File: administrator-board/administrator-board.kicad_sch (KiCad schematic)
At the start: 10 parts, among them J2 Conn_01x06, J3 Conn_01x06, SW2 SW_Push, SW3 SW_Push, SW4 SW_Push, SW5 SW_Push

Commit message: フットプリントの割り当て
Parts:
- J2, J3: footprint (none) -> Connector_JST:JST_XH_S6B-XH-A_1x06_P2.50mm_Horizontal
- R2, R3, R4, R5: footprint (none) -> Resistor_SMD:R_0603_1608Metric_Pad0.98x0.95mm_HandSolder
- SW2, SW3, SW4, SW5: footprint (none) -> Button_Switch_THT:SW_PUSH_6mm
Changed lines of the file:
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@@
 			)
 		)
-		(property "Footprint" ""
+		(property "Footprint" "Connector_JST:JST_XH_S6B-XH-A_1x06_P2.50mm_Horizontal"
 			(at 177.8 146.05 0)
 			(hide yes)
@@
 			)
 		)
-		(property "Footprint" ""
+		(property "Footprint" "Resistor_SMD:R_0603_1608Metric_Pad0.98x0.95mm_HandSolder"
 			(at 211.582 110.49 90)
 			(hide yes)
@@
 			)
 		)
-		(property "Footprint" ""
+		(property "Footprint" "Resistor_SMD:R_0603_1608Metric_Pad0.98x0.95mm_HandSolder"
 			(at 160.782 110.49 90)
 			(hide yes)
@@
 			)
 		)
-		(property "Footprint" ""
+		(property "Footprint" "Resistor_SMD:R_0603_1608Metric_Pad0.98x0.95mm_HandSolder"
 			(at 188.722 110.49 90)
 			(hide yes)
@@
 			)
 		)
-		(property "Footprint" ""
+		(property "Footprint" "Button_Switch_THT:SW_PUSH_6mm"
 			(at 195.58 99.06 0)
 			(hide yes)
@@
 			)
 		)
-		(property "Footprint" ""
+		(property "Footprint" "Connector_JST:JST_XH_S6B-XH-A_1x06_P2.50mm_Horizontal"
 			(at 219.71 144.78 0)
 			(hide yes)
@@
 			)
 		)
-		(property "Footprint" ""
+		(property "Footprint" "Button_Switch_THT:SW_PUSH_6mm"
 			(at 241.3 99.06 0)
 			(hide yes)
@@
 			)
 		)
-		(property "Footprint" ""
+		(property "Footprint" "Resistor_SMD:R_0603_1608Metric_Pad0.98x0.95mm_HandSolder"
 			(at 234.442 110.49 90)
 			(hide yes)
@@
 			)
 		)
-		(property "Footprint" ""
+		(property "Footprint" "Button_Switch_THT:SW_PUSH_6mm"
 			(at 167.64 99.06 0)
 			(hide yes)
@@
 			)
 		)
-		(property "Footprint" ""
+		(property "Footprint" "Button_Switch_THT:SW_PUSH_6mm"
 			(at 218.44 99.06 0)
 			(hide yes)

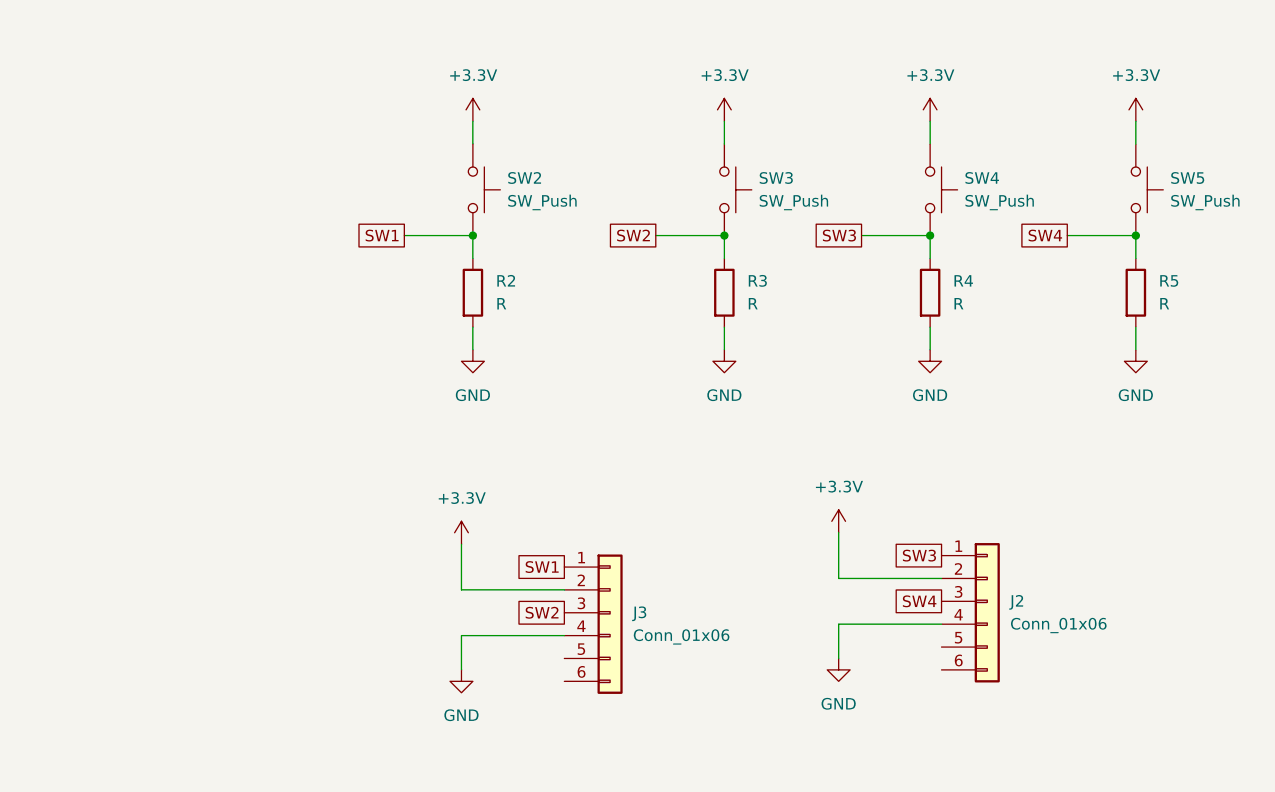
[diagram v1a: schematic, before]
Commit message: LED追加
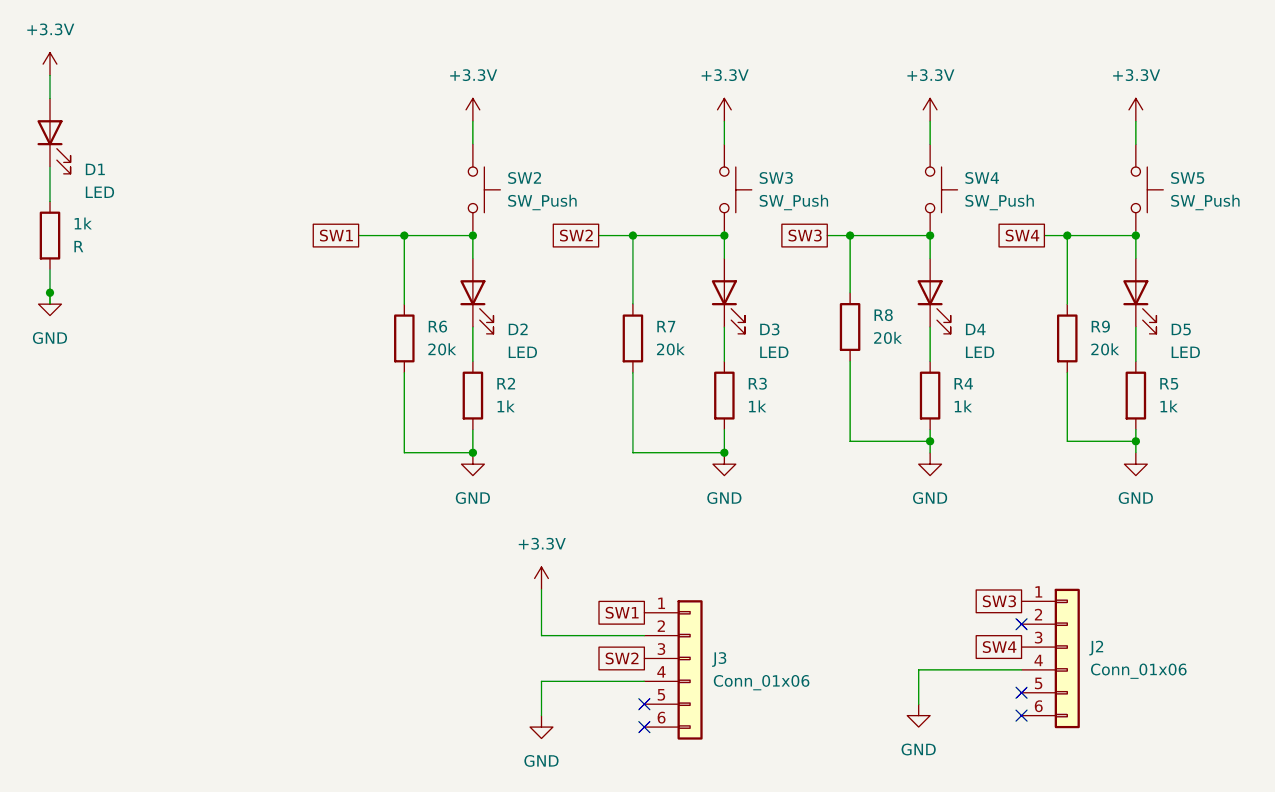
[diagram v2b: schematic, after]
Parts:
- added 1k: R, Resistor_SMD:R_0603_1608Metric_Pad0.98x0.95mm_HandSolder, symbol Device:R
- added D1, D2, D3, D4, D5: LED, symbol Device:LED
- added R6, R7, R8, R9: 20k, Resistor_SMD:R_0603_1608Metric_Pad0.98x0.95mm_HandSolder, symbol Device:R
- R2, R3, R4, R5: value R -> 1k
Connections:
- net +3.3V: now also D1.2 (A); no longer J2.2 (Pin_2)
- net GND: now also 1k.2, R6.2, R7.2, R8.2, R9.2
- net SW1: now also D2.2 (A), R6.1; no longer R2.1
- net SW2: now also D3.2 (A), R7.1; no longer R3.1
- net SW3: now also D4.2 (A), R8.1; no longer R4.1
- net SW4: now also D5.2 (A), R9.1; no longer R5.1
- new net: D4.1 (K), R4.1
- new net: D3.1 (K), R3.1
- new net: 1k.1, D1.1 (K)
- new net: D2.1 (K), R2.1
- new net: D5.1 (K), R5.1
- no-connect marks 0 -> 5
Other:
- moved on the sheet: J2, J3, R2, R3, R4, R5

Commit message: GNDの色塗りまで終わった
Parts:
- D1, D2, D3, D4, D5: footprint (none) -> LED_SMD:LED_0603_1608Metric_Pad1.05x0.95mm_HandSolder
- R1: renamed from 1k; value R -> 1k
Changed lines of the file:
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@@
 			)
 		)
-		(property "Footprint" ""
+		(property "Footprint" "LED_SMD:LED_0603_1608Metric_Pad1.05x0.95mm_HandSolder"
 			(at 190.5 110.49 0)
 			(hide yes)
@@
 		(dnp no)
 		(fields_autoplaced yes)
-		(property "Reference" "1k"
+		(property "Reference" "R1"
 			(at 118.11 102.8699 0)
 			(show_name no)
@@
 			)
 		)
-		(property "Value" "R"
+		(property "Value" "1k"
 			(at 118.11 105.4099 0)
 			(show_name no)
@@
 			(project "administrator-board"
 				(path "/d3296edd-98d5-4d49-a411-50c326b4086d"
-					(reference "1k")
+					(reference "R1")
 					(unit 1)
 				)
@@
 			)
 		)
-		(property "Footprint" ""
+		(property "Footprint" "LED_SMD:LED_0603_1608Metric_Pad1.05x0.95mm_HandSolder"
 			(at 115.57 92.71 0)
 			(hide yes)
@@
 			)
 		)
-		(property "Footprint" ""
+		(property "Footprint" "LED_SMD:LED_0603_1608Metric_Pad1.05x0.95mm_HandSolder"
 			(at 162.56 110.49 0)
 			(hide yes)
@@
 			)
 		)
-		(property "Footprint" ""
+		(property "Footprint" "LED_SMD:LED_0603_1608Metric_Pad1.05x0.95mm_HandSolder"
 			(at 236.22 110.49 0)
 			(hide yes)
@@
 			)
 		)
-		(property "Footprint" ""
+		(property "Footprint" "LED_SMD:LED_0603_1608Metric_Pad1.05x0.95mm_HandSolder"
 			(at 213.36 110.49 0)
 			(hide yes)
